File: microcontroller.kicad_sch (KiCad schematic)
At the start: 30 parts, among them J9 Conn_01x02_Socket, U3 RP2350A, X1 ABM8-272-T3

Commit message: Placement
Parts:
- removed J9: Conn_01x02_Socket, Connector_JST:JST_PH_B2B-PH-K_1x02_P2.00mm_Vertical, symbol Connector:Conn_01x02_Socket
- added R3: 1k, Resistor_SMD:R_0603_1608Metric, symbol Device:R
- renumbered C11 to C10, C10 to C11, R9 to R10, R10 to R11, R11 to R12, R12 to R13, R5 to R4, R6 to R5, R3 to R6, R4 to R7, R7 to R8, R8 to R9
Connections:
- net GND: now also R3.1; no longer U3.12 (GPIO8), U3.13 (GPIO9), U3.17 (GPIO13), U3.18 (GPIO14), U3.19 (GPIO15), U3.7 (GPIO4), U3.8 (GPIO5)
- net nSHDN: now also R3.2
- no-connect marks 21 -> 28

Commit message: Doing placement
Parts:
- added D15, D16, D17: LED, LED_SMD:LED_0603_1608Metric, symbol Device:LED
- added R25, R26, R27: R, Resistor_SMD:R_0603_1608Metric, symbol Device:R
- R10, R8: value 1k -> 10k; Mfr P/N AC0603FR-071KL -> RT0603BRD0710KL; Supplier_1 P/N 311-1KLDTR-ND -> YAG1236TR-ND; Supplier_1 Unit Price 0.10000 -> 0.11; Supplier_2 P/N C116692 -> C95204; Supplier_2 Unit Price 0.0025 -> 0.0216
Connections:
- net QSPI_SS is gone; now on net +3V3: R10.1, U3.60 (QSPI_SS)
- net +3V3: now also R3.1, R4.1, R5.2, R8.2, U3.26 (RUN), U3.31 (GPIO19), U3.32 (GPIO20), U3.33 (GPIO21), D15.2 (A), D16.2 (A), D17.2 (A)
- net GND: now also R25.2, R26.2, R27.2; no longer R3.1, R4.1, R5.2
- new net: D17.1 (K), R27.1
- new net: D16.1 (K), R26.1
- new net: D15.1 (K), R25.1
- no-connect marks 28 -> 25
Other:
- note removed: "EPAD Stitching"
- moved on the sheet: C1, C10, C11, C12, C13, C14, C15, C16, C2, C3, C4, C5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

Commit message: Did a lot of routing
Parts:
- L1: footprint Inductor_SMD:L_0805_2012Metric -> _BMS:rp_inductor
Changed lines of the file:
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@@
 			)
 		)
-		(property "Footprint" "Inductor_SMD:L_0805_2012Metric"
+		(property "Footprint" "_BMS:rp_inductor"
 			(at 314.96 124.46 0)
 			(effects

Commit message: Working on routing
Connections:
- net +3V3: now also R25.1, R26.1, R27.1; no longer D15.2 (A), D16.2 (A), D17.2 (A), U3.31 (GPIO19), U3.32 (GPIO20), U3.33 (GPIO21)
- net GND: now also D15.1 (K), D16.1 (K), D17.1 (K); no longer R25.2, R26.2, R27.2
- new net LED1: D15.2 (A), R25.2, U3.33 (GPIO21)
- new net LED2: D16.2 (A), R26.2, U3.32 (GPIO20)
- new net LED3: D17.2 (A), R27.2, U3.31 (GPIO19)
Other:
- moved on the sheet: R25, R26, R27

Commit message: Pushing
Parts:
- added C24: 100 nF, Capacitor_SMD:C_0603_1608Metric, symbol Device:C
- added R22: 10k, Resistor_SMD:R_0603_1608Metric, symbol Device:R
- added R34, R35: 33k, Resistor_SMD:R_0603_1608Metric, symbol Device:R
- added U12: W25Q64JVSSIQ, _BMS:SOIC-8_5P28X5P28_WIN, symbol _W25Q64JVSSIQ:W25Q64JVSSIQ
- R10, R8: value 10k -> 1k; Mfr P/N RT0603BRD0710KL -> RC0603FR-071KL; Supplier_1 Digikey -> (none); Supplier_1 P/N YAG1236TR-ND -> (none); Supplier_1 Price @ Qty 1 -> (none); Supplier_1 Unit Price 0.11 -> (none); Supplier_2 P/N C95204 -> C22548; Supplier_2 Unit Price 0.0216 -> 0.0014
- U3: footprint _BMS:QFN-60_7X7_RPI -> Package_DFN_QFN:QFN-60-1EP_7x7mm_P0.4mm_EP3.4x3.4mm_ThermalVias; Supplier_2 (none) -> JLCPCB; Supplier_2 P/N (none) -> C42411118; Supplier_2 Price @ Qty (none) -> 1; Supplier_2 Unit Price (none) -> 1.25
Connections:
- net +1V1: now also C11.1; no longer C11.2
- net +3V3: now also C13.1, C9.1, C24.2, R22.1, R34.1, R35.2, U12.8 (VCC); no longer C13.2, C9.2, R10.1, R8.2, U3.26 (RUN), U3.60 (QSPI_SS)
- net BOOT: now also R10.1; no longer R10.2
- net GND: now also C11.2, C13.2, C9.2, C24.1, U12.4 (GND); no longer C11.1, C13.1, C9.1
- net SCL: now also U3.35 (GPIO23), R35.1; no longer R5.1, U3.10 (GPIO7)
- net SDA: now also U3.34 (GPIO22), R34.2; no longer R4.2, U3.9 (GPIO6)
- net QSPI_SD3: now reaches U3.55 (QSPI_SD3)
- net QSPI_SD3: now also U12.7 (/HOLD_OR_/RESET(IO3))
- net QSPI_SCLK: now reaches U3.56 (QSPI_SCLK)
- net QSPI_SCLK: now also U12.6 (CLK)
- net QSPI_SD0: now reaches U3.57 (QSPI_SD0)
- net QSPI_SD0: now also U12.5 (DI(IO0))
- net QSPI_SD2: now reaches U3.58 (QSPI_SD2)
- net QSPI_SD2: now also U12.3 (/WP(IO2))
- net QSPI_SD1: now reaches U3.59 (QSPI_SD1)
- net QSPI_SD1: now also U12.2 (DO(IO1))
- new net: R8.2, U3.26 (RUN)
- new net QSPI_SS: R10.2, R22.2, U12.1 (/CS), U3.60 (QSPI_SS)
- new net SCL0: R5.1, U3.10 (GPIO7)
- new net SDA0: R4.2, U3.9 (GPIO6)
- no-connect marks 25 -> 18
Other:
- note added: "I2C0 bus for external comms"
- note added: "I2C1 bus for communciation with MP2790"
- moved on the sheet: C11, C12, C13, C14, C9, R10, R11, R12, R13, R3, R4, R5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

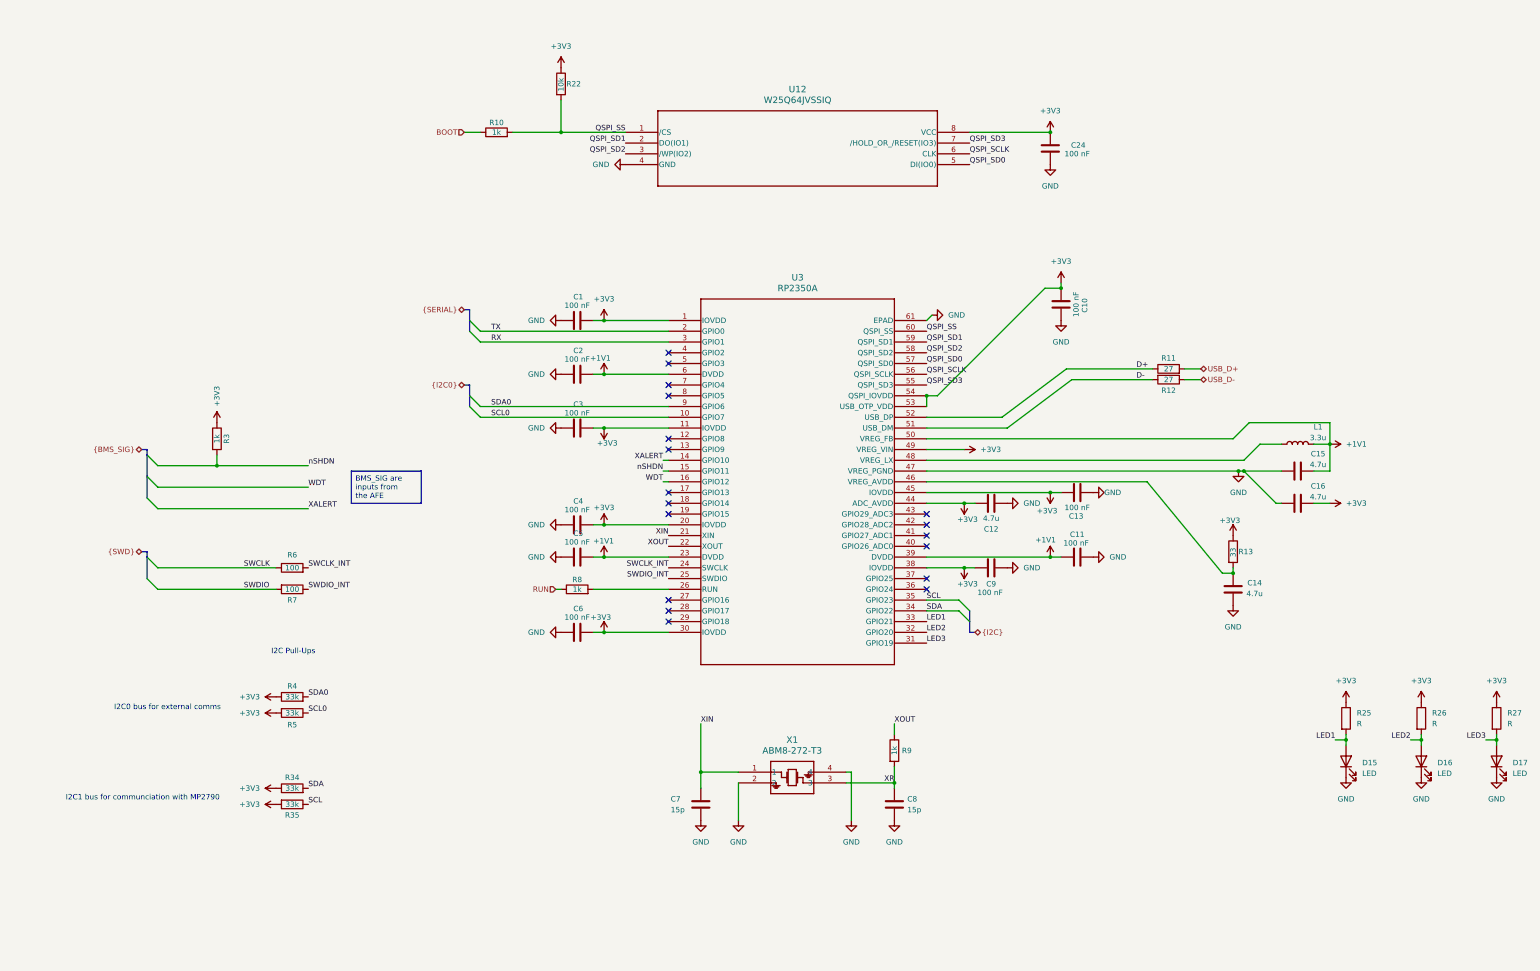
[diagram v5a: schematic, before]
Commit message: Adding in signals and cleaning up schematic
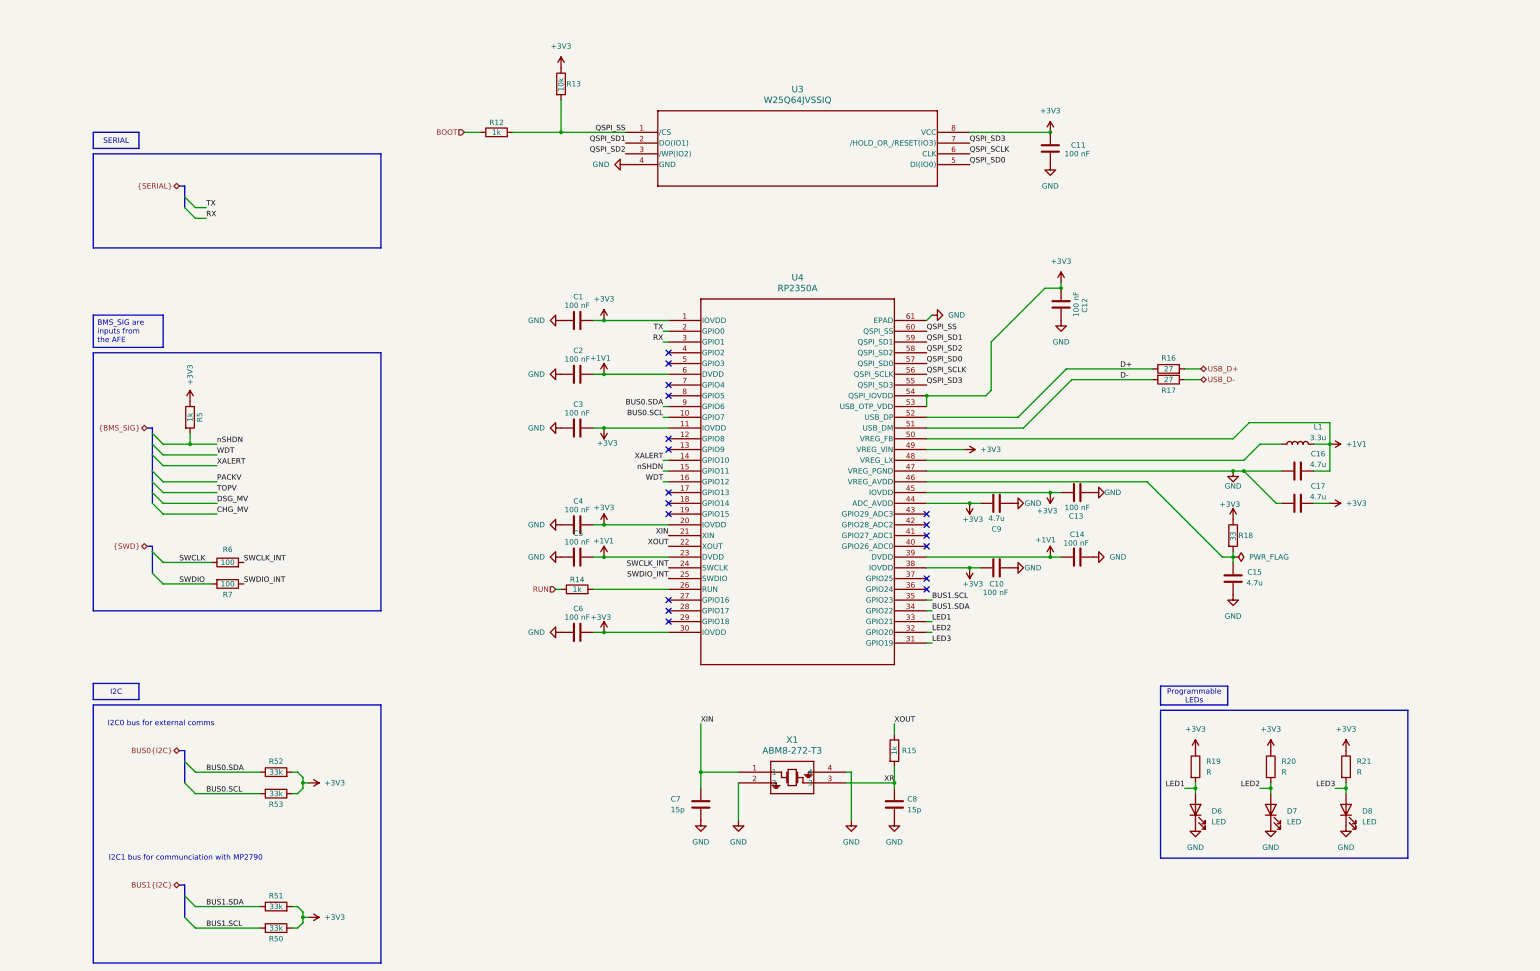
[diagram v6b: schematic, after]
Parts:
- removed R34, R35, R4, R5: 33k, Resistor_SMD:R_0603_1608Metric, symbol Device:R
- added R50, R51, R52, R53: 33k, Resistor_SMD:R_0603_1608Metric, symbol Device:R
- renumbered C9 to C10, C24 to C11, C10 to C12, C11 to C14, C14 to C15, C15 to C16, C16 to C17, C12 to C9, D15 to D6, D16 to D7, D17 to D8, R10 to R12, R22 to R13, R8 to R14, R9 to R15, R11 to R16, R12 to R17, R13 to R18, R25 to R19, R26 to R20, R27 to R21, R3 to R5, U12 to U3, U3 to U4
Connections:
- net +3V3: now also R50.1, R51.2, R52.2, R53.1
- net SCL renamed BUS1.SCL
- net BUS1.SCL: now also R50.2
- net SCL0 renamed BUS0.SCL
- net BUS0.SCL: now also R53.2
- net SDA renamed BUS1.SDA
- net BUS1.SDA: now also R51.1
- net SDA0 renamed BUS0.SDA
- net BUS0.SDA: now also R52.1
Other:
- note removed: "I2C Pull-Ups"
- moved on the sheet: C10, C15, C9, D6, D7, D8, R18, R19, R20, R21, R5, R6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

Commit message: Redoing layout
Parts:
- C12: footprint Capacitor_SMD:C_0603_1608Metric -> Capacitor_SMD:C_0201_0603Metric
- R16, R17: footprint Resistor_SMD:R_0603_1608Metric -> Resistor_SMD:R_0201_0603Metric
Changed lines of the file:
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@@
 			)
 		)
-		(property "Footprint" "Resistor_SMD:R_0603_1608Metric"
+		(property "Footprint" "Resistor_SMD:R_0201_0603Metric"
 			(at 284.48 108.458 90)
 			(effects
@@
 			)
 		)
-		(property "Footprint" "Capacitor_SMD:C_0603_1608Metric"
+		(property "Footprint" "Capacitor_SMD:C_0201_0603Metric"
 			(at 258.1148 87.63 0)
 			(effects
@@
 			)
 		)
+		(property "Supplier_1 Price @ Qty" ""
+			(at 259.08 91.44 0)
+			(effects
+				(font
+					(size 1.27 1.27)
+				)
+				(hide yes)
+			)
+		)
+		(property "Supplier_2 Price @ Qty" ""
+			(at 259.08 91.44 0)
+			(effects
+				(font
+					(size 1.27 1.27)
+				)
+				(hide yes)
+			)
+		)
 		(pin "2"
 		)
@@
 			)
 		)
-		(property "Footprint" "Resistor_SMD:R_0603_1608Metric"
+		(property "Footprint" "Resistor_SMD:R_0201_0603Metric"
 			(at 284.48 107.442 90)
 			(effects

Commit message: prepaing for production
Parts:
- C12: Mfr YAGEO -> (none); Mfr P/N CC0603JRX7R9BB104 -> (none); Supplier_1 DigiKey -> (none); Supplier_1 P/N 311-1779-2-ND -> (none); Supplier_1 Price @ QTY 1 -> (none); Supplier_1 Unit Price 0.10000 -> (none); Supplier_2 JLCPCB -> (none); Supplier_2 P/N C91183 -> (none); Supplier_2 Price @ QTY 1 -> (none)
- D3: renamed from D6; Mfr (none) -> Vishay Intertech; Mfr P/N (none) -> VLMW1300-GS08; Supplier_2 (none) -> JLCPCB; Supplier_2 P/N (none) -> C413463
- D4: renamed from D7; Mfr (none) -> Vishay Intertech; Mfr P/N (none) -> VLMW1300-GS08; Supplier_2 (none) -> JLCPCB; Supplier_2 P/N (none) -> C413463
- D5: renamed from D8; Mfr (none) -> Vishay Intertech; Mfr P/N (none) -> VLMW1300-GS08; Supplier_2 (none) -> JLCPCB; Supplier_2 P/N (none) -> C413463
- L1: Supplier_2 (none) -> JLCPCB; Supplier_2 P/N (none) -> C42411119
- R16, R17: Supplier_2 (none) -> JLCPCB; Supplier_2 P/N (none) -> C861276
- R18: renamed from R19; value R -> 470; Mfr (none) -> YAGEO; Mfr P/N (none) -> RC0603FR-07470RL; Supplier_2 (none) -> JLCPCB; Supplier_2 P/N (none) -> C114669
- R20, R21: value R -> 470; Mfr (none) -> YAGEO; Mfr P/N (none) -> RC0603FR-07470RL; Supplier_2 (none) -> JLCPCB; Supplier_2 P/N (none) -> C114669
- X1: Supplier_2 (none) -> JLCPCB; Supplier_2 P/N (none) -> C20625731
- renumbered R51 to R10, R50 to R11, R18 to R19, R52 to R8, R53 to R9, U3 to U2, U4 to U3
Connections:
- net +3V3: no longer R18.1, R20.1, R21.1
- net CHG_MV: now also U3.40 (GPIO26_ADC0)
- net DSG_MV: now also U3.41 (GPIO27_ADC1)
- net LED1: now also R18.1; no longer D3.2 (A), R18.2
- net LED2: now also R20.1; no longer D4.2 (A), R20.2
- net LED3: now also R21.1; no longer D5.2 (A), R21.2
- net PACKV: now also U3.43 (GPIO29_ADC3)
- net TOPV: now also U3.42 (GPIO28_ADC2)
- net GPIO1: now reaches U3.17 (GPIO13)
- net GPIO2: now reaches U3.18 (GPIO14)
- new net: D5.2 (A), R21.2
- new net: D4.2 (A), R20.2
- new net: D3.2 (A), R18.2
- no-connect marks 18 -> 12
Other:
- moved on the sheet: D3, D4, D5, R18, R20, R21, R5
